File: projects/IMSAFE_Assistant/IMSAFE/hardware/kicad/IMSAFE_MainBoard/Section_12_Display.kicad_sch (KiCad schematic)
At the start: 0 parts

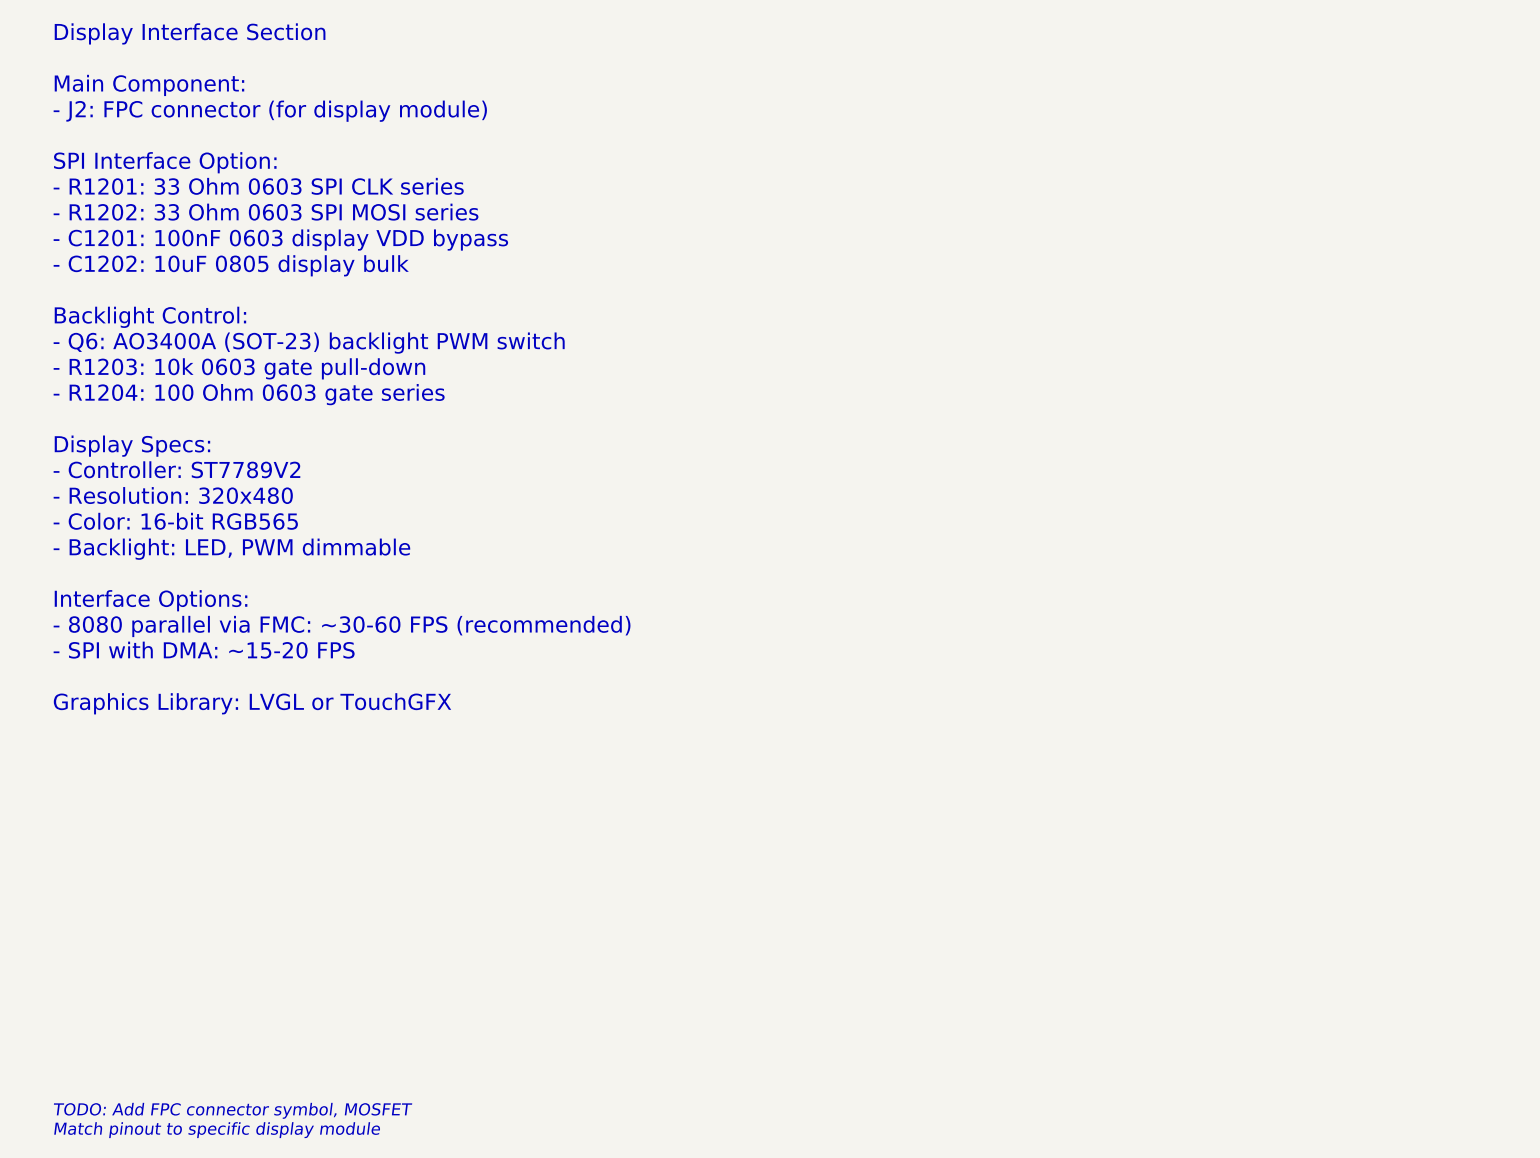
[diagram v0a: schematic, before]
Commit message: Update KiCad schematics and add analysis files
- Update all MainBoard schematic sections with component placement
- Add ERC reports and analysis scripts for schematic validation
- Update Radar Interface and SwitchLED Board projects
- Sync KiCad project files with latest session changes

Co-Authored-By: Claude Opus 4.5 <noreply@anthropic.com>
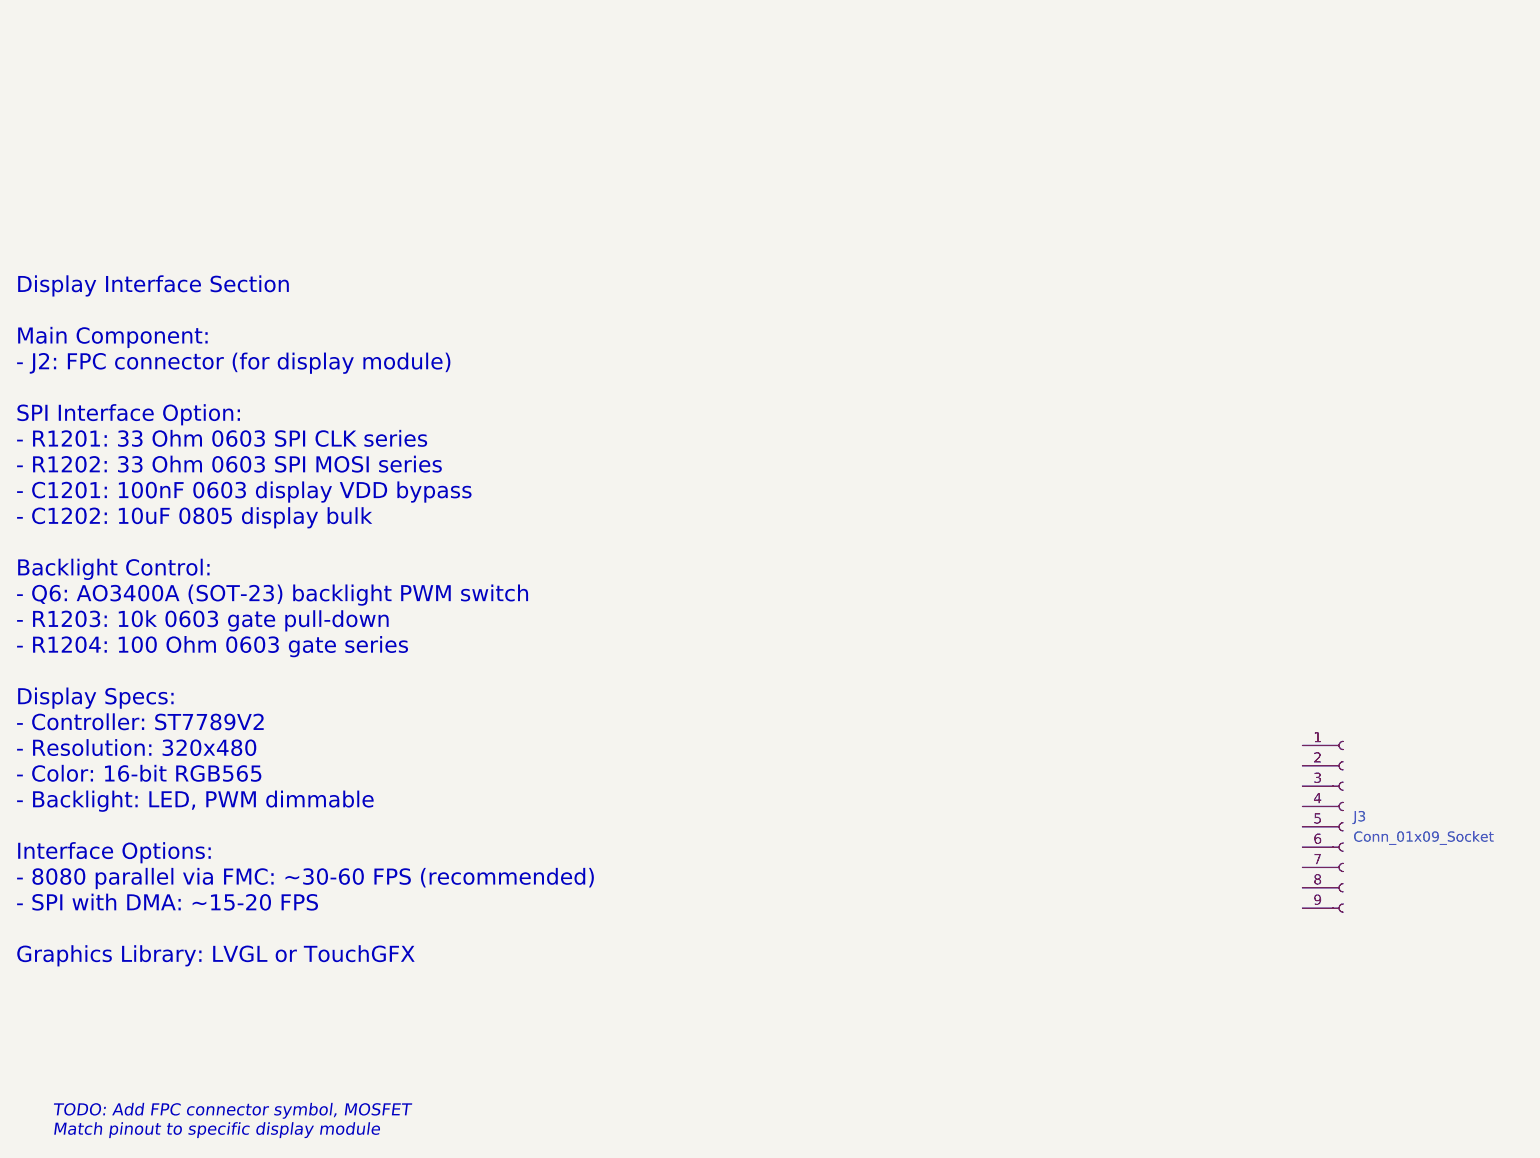
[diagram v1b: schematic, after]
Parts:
- added J3: Conn_01x09_Socket, symbol Connector:Conn_01x09_Socket
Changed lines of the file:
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@@
 (kicad_sch
-	(version 20231120)
+	(version 20250114)
 	(generator "eeschema")
-	(generator_version "8.0")
-	(uuid "sec12-0001-0002-0003-000000000001")
+	(generator_version "9.0")
 	(paper "A4")
 	(title_block
@@
 	(text "Display Interface Section\n\nMain Component:\n- J2: FPC connector (for display module)\n\nSPI Interface Option:\n- R1201: 33 Ohm 0603 SPI CLK series\n- R1202: 33 Ohm 0603 SPI MOSI series\n- C1201: 100nF 0603 display VDD bypass\n- C1202: 10uF 0805 display bulk\n\nBacklight Control:\n- Q6: AO3400A (SOT-23) backlight PWM switch\n- R1203: 10k 0603 gate pull-down\n- R1204: 100 Ohm 0603 gate series\n\nDisplay Specs:\n- Controller: ST7789V2\n- Resolution: 320x480\n- Color: 16-bit RGB565\n- Backlight: LED, PWM dimmable\n\nInterface Options:\n- 8080 parallel via FMC: ~30-60 FPS (recommended)\n- SPI with DMA: ~15-20 FPS\n\nGraphics Library: LVGL or TouchGFX"
 		(exclude_from_sim no)
-		(at 25.4 25.4 0)
+		(at 20.828 56.896 0)
 		(effects
 			(font
@@
 			(justify left)
 		)
-		(uuid "sec12-text-001")
 	)
 	(text "TODO: Add FPC connector symbol, MOSFET\nMatch pinout to specific display module"
@@
 			(justify left)
 		)
-		(uuid "sec12-todo-001")
+	)
+	(symbol
+		(lib_id "Connector:Conn_01x09_Socket")
+		(at 186.69 82.55 0)
+		(unit 1)
+		(exclude_from_sim no)
+		(in_bom yes)
+		(on_board yes)
+		(dnp no)
+		(fields_autoplaced yes)
+		(property "Reference" "J3"
+			(at 187.96 81.2799 0)
+			(effects
+				(font
+					(size 1.27 1.27)
+				)
+				(justify left)
+			)
+		)
+		(property "Value" "Conn_01x09_Socket"
+			(at 187.96 83.8199 0)
+			(effects
+				(font
+					(size 1.27 1.27)
+				)
+				(justify left)
+			)
+		)
+		(property "Footprint" ""
+			(at 186.69 82.55 0)
+			(effects
+				(font
+					(size 1.27 1.27)
+				)
+				(hide yes)
+			)
+		)
+		(property "Datasheet" "~"
+			(at 186.69 82.55 0)
+			(effects
+				(font
+					(size 1.27 1.27)
+				)
+				(hide yes)
+			)
+		)
+		(property "Description" "Generic connector, single row, 01x09, script generated"
+			(at 186.69 82.55 0)
+			(effects
+				(font
+					(size 1.27 1.27)
+				)
+				(hide yes)
+			)
+		)
+		(pin "2"
+		)
+		(pin "1"
+		)
+		(pin "5"
+		)
+		(pin "3"
+		)
+		(pin "4"
+		)
+		(pin "6"
+		)
+		(pin "7"
+		)
+		(pin "8"
+		)
+		(pin "9"
+		)
+		(instances
+			(project ""
+				(path "/a1b2c3d4-e5f6-7890-abcd-ef1234567890/245953ab-4da3-4029-b8f2-0b0c87ffcc3e"
+					(reference "J3")
+					(unit 1)
+				)
+			)
+		)
 	)
 )
